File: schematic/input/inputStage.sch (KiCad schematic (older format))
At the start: 37 parts, among them IC1 LM361N_NOPB, IC2 ADA4891-2ARMZ-R7, J1 Screw_Terminal_01x04, J2 Screw_Terminal_01x04, U1 LM324, U2 LM7805_TO220

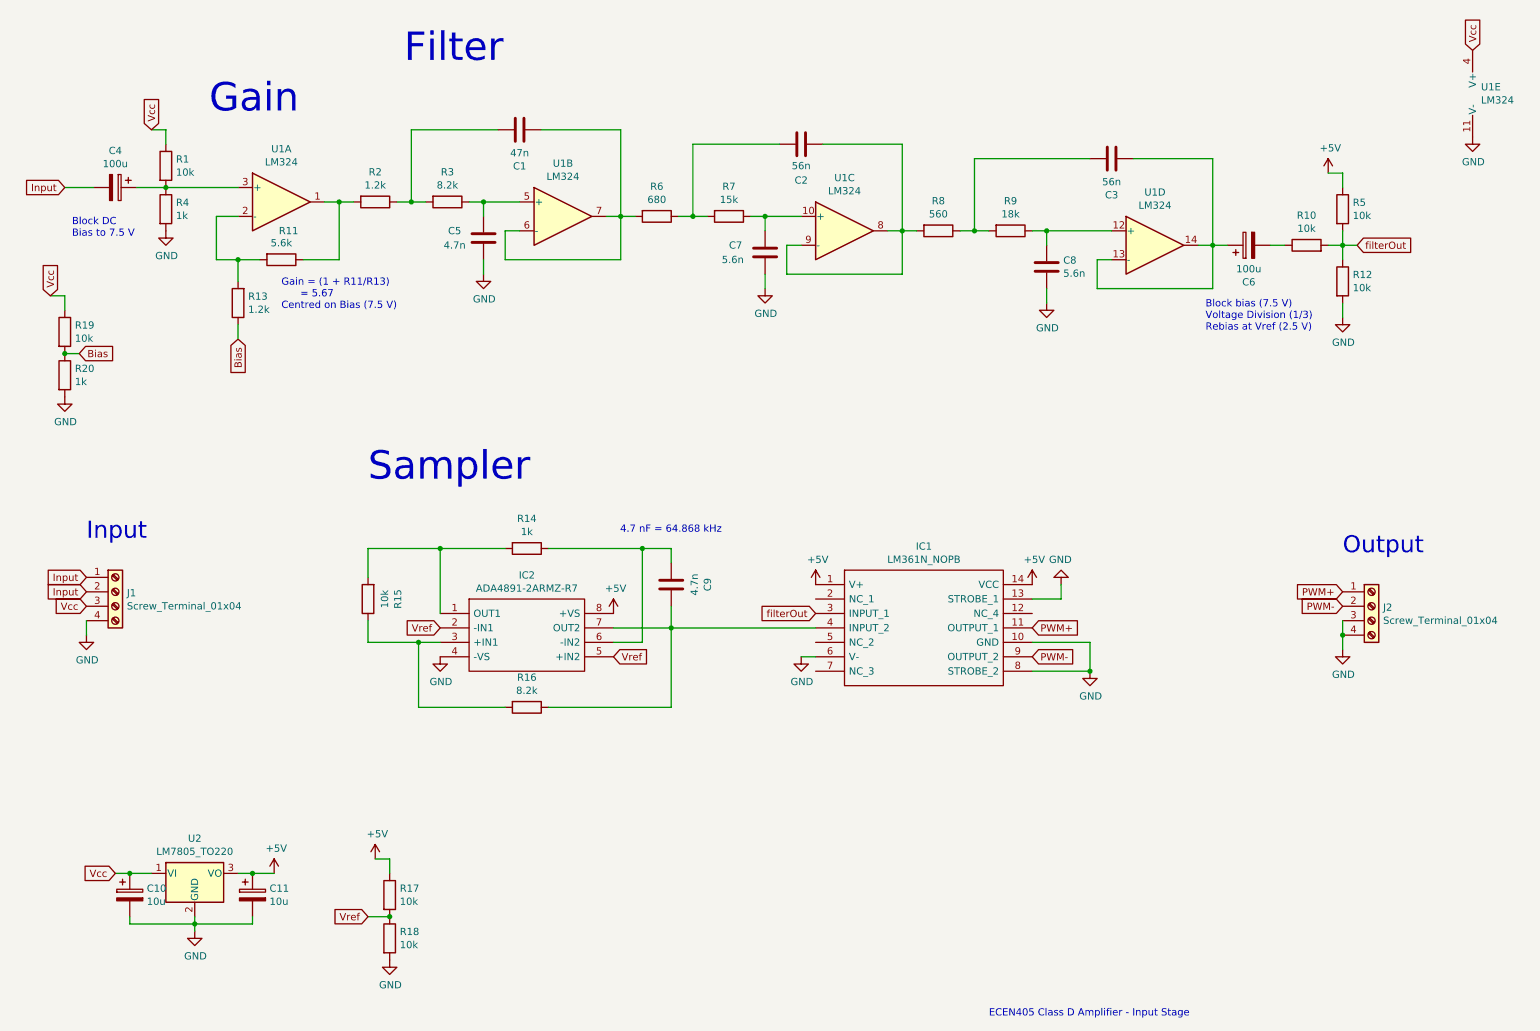
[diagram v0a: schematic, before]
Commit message: Added small decoupling caps
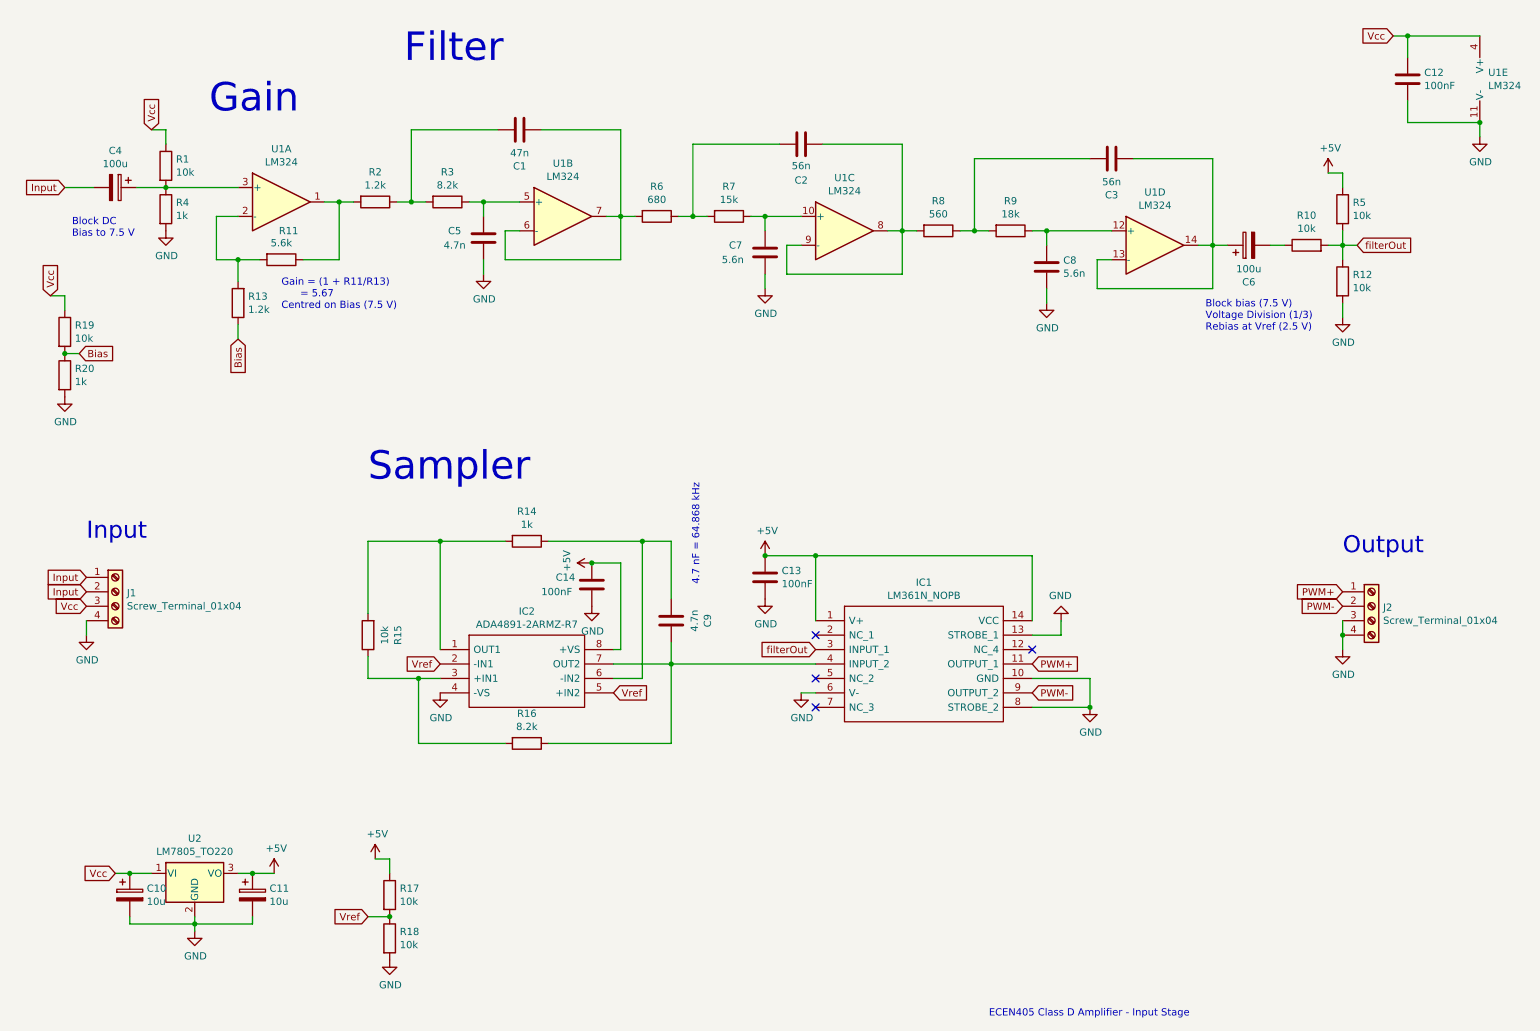
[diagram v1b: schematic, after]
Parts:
- added C12, C13, C14: 100nF, Capacitor_THT:C_Disc_D5.0mm_W2.5mm_P5.00mm, symbol Device:C
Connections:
- net +5V: now also C13.1, C14.1
- net GND: now also C12.2, C13.2, C14.2
- net Vcc: now also C12.1
- no-connect marks 0 -> 4
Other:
- moved on the sheet: C9, IC1, IC2, R14, R15, R16, U1E

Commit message: Updated terminals and added IC labels
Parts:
- J1, J2: footprint TerminalBlock_TE-Connectivity:TerminalBlock_TE_282834-4_1x04_P2.54mm_Horizontal -> TerminalBlock_Phoenix:TerminalBlock_Phoenix_PT-1,5-4-3.5-H_1x04_P3.50mm_Horizontal
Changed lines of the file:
@@
 F 0 "J1" H 1430 4542 50  0000 L CNN
 F 1 "Screw_Terminal_01x04" H 1430 4451 50  0000 L CNN
-F 2 "TerminalBlock_TE-Connectivity:TerminalBlock_TE_282834-4_1x04_P2.54mm_Horizontal" H 1350 4550 50  0001 C CNN
+F 2 "TerminalBlock_Phoenix:TerminalBlock_Phoenix_PT-1,5-4-3.5-H_1x04_P3.50mm_Horizontal" H 1350 4550 50  0001 C CNN
 F 3 "~" H 1350 4550 50  0001 C CNN
 	1    1350 4550
@@
 F 0 "J2" H 10130 4642 50  0000 L CNN
 F 1 "Screw_Terminal_01x04" H 10130 4551 50  0000 L CNN
-F 2 "TerminalBlock_TE-Connectivity:TerminalBlock_TE_282834-4_1x04_P2.54mm_Horizontal" H 10050 4650 50  0001 C CNN
+F 2 "TerminalBlock_Phoenix:TerminalBlock_Phoenix_PT-1,5-4-3.5-H_1x04_P3.50mm_Horizontal" H 10050 4650 50  0001 C CNN
 F 3 "~" H 10050 4650 50  0001 C CNN
 	1    10050 4650

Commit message: Terminal updates
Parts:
- R4: value 1k -> 10k
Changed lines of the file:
@@
 P 1700 1900
 F 0 "R4" H 1770 1946 50  0000 L CNN
-F 1 "1k" H 1770 1855 50  0000 L CNN
+F 1 "10k" H 1770 1855 50  0000 L CNN
 F 2 "Resistor_THT:R_Axial_DIN0207_L6.3mm_D2.5mm_P10.16mm_Horizontal" V 1630 1900 50  0001 C CNN
 F 3 "~" H 1700 1900 50  0001 C CNN
